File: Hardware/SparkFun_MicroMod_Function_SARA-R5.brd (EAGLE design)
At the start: 37.5 x 65 mm, 104 parts, among them IC2 SN74AVC4T774PW, J1 MICROMOD_FUNCTION_STANDARD, J2 U.FL, J5 U.FL, J9 NANO_SIM, Q2 310mA/60V/1.6Ω, Q3 310mA/60V/1.6Ω, Q5 310mA/60V/1.6Ω, Q6 310mA/60V/1.6Ω, U11 74HC1G04, U4 EEPROM, U6 LARA-R6001, U8 AP7361C-33FGE

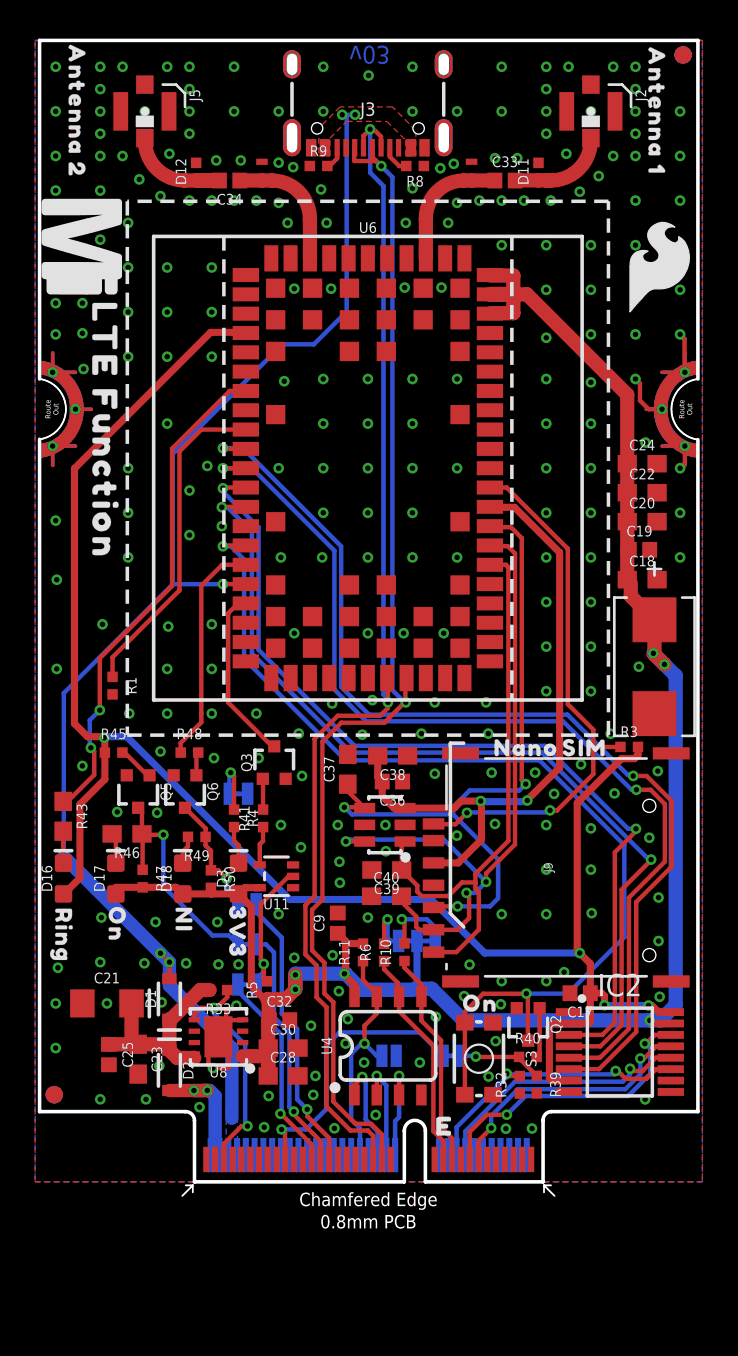
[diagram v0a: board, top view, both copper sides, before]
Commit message: added GNSS antenna U.FL
-added GNSS antenna U.FL, with supporting circuitry and power control
-rotated module 90 degrees
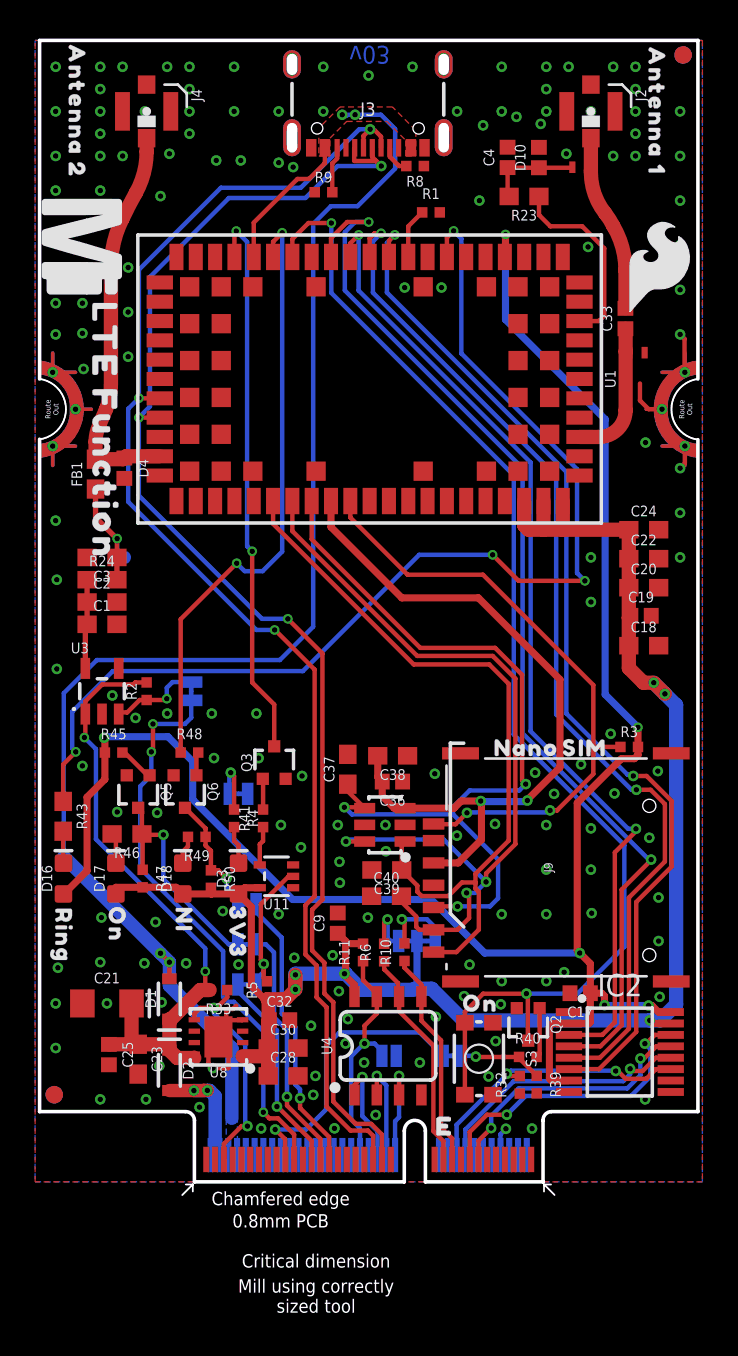
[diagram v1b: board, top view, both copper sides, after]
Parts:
- removed C16: T520D337M006ATE045, untitled:CAPMP7.6X4.3_3.1N_KEM
- removed C34: 33pF, New_Parts:0402
- removed D11, D12: PESD0402-0402T, SparkFun-DiscreteSemi:0402-TIGHT
- removed J5: U.FL, SparkFun-Connectors:U.FL
- removed U6: LARA-R6001, HPG_Solution:LARA-LGA
- added C1: 1.0uF, SparkFun-Capacitors:0603
- added C2: 0.1uF, SparkFun-Capacitors:0603
- added C3: 47pF, SparkFun-Capacitors:0603
- added C4: 27pF, New_Parts:0402
- added D10, D4: PESD0402, New_Parts:0402
- added FB1: 30Ω/1.8A, SparkFun-Coils:0603
- added J4: U.FL, SparkFun-Connectors:U.FL
- added JP4: JUMPER-SMT_2_NC_TRACE_SILK, SparkFun-Jumpers:SMT-JUMPER_2_NC_TRACE_SILK
- added R2: 100k, SparkFun-Resistors:0402-TIGHT
- added R23: 10k, SparkFun-Resistors:0603
- added R24: 10, SparkFun-Resistors:0603
- added TP22: TEST-POINT3, SparkFun-Connectors:PAD.03X.03
- added U1: SARA-R510M8S, SparkFun-RF:SARA-LGA
- added U3: 3.3V, SparkFun-IC-Power:SOT23-5
- JP3: value JUMPER-SMT_2_NO_SILK -> (none)
- L2: value DNP -> 68nH
- R46: device SparkFun-Resistors:0603 -> SparkFun-Resistors:0603@1
- moved R1 32.5 mm to (22.5, 55.2), turned to 0 degrees
- moved L2 18.1 mm to (31.0, 57.8), turned to 0 degrees
- moved L1 14.1 mm to (34.3, 47.2), turned to 0 degrees
- moved C33 10.4 mm to (33.6, 49.2), turned to 90 degrees
- moved C22 3.76 mm to (34.7, 35.5)
- moved C18 3.76 mm to (34.7, 30.5)
- moved C19 3.76 mm to (34.5, 32.2)
- moved C20 3.76 mm to (34.7, 33.8)
- moved C24 3.76 mm to (34.7, 37.1)
- moved R9 1.52 mm to (16.4, 56.4)
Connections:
- removed net LTE_ANT2: C34.1, L2.P$1, U6.62
- removed net N$10: C21.+, C23.1, C25.1, D1.C, D2.C, R33.2, U8.8
- removed net N$15: C33.2, D11.1, J2.FEED
- new net ANT_REG_EN: JP4.1, R2.1, U3.3
- new net GNSS_ANT: D4.1, FB1.2, J4.FEED, U1.31
- new net N$11: C33.2, J2.FEED, L2.P$2
- new net N$18: C4.1, D10.1, L2.P$1, R23.2
- new net N$24: C1.1, C2.1, R24.1, U3.5
- new net N$25: C3.1, FB1.1, R24.2, TP22.P$1
- new net SARA_ANT_DET: R23.1, U1.62
- new net VIN: C21.+, C23.1, C25.1, D1.C, D2.C, R2.2, R33.2, U3.1, U8.8
- net 3.3V: now also U1.51, U1.52, U1.53; no longer C16.1, U6.51, U6.52, U6.53
- net GND: now also C1.2, C2.2, C3.2, C4.2, D10.2, D4.2, J1.2, J1.8, J4.1, J4.2, U1.1, U1.14, U1.20, U1.21, U1.22, U1.3, U1.30, U1.32, U1.43, U1.5, U1.50, U1.54, U1.55, U1.57, U1.58, U1.59, U1.60, U1.61, U1.63, U1.64, U1.65, U1.66, U1.67, U1.68, U1.69, U1.70, U1.71, U1.72, U1.73, U1.74, U1.75, U1.76, U1.77, U1.78, U1.79, U1.80, U1.81, U1.82, U1.83, U1.84, U1.85, U1.86, U1.87, U1.88, U1.89, U1.90, U1.91, U1.92, U1.93, U1.94, U1.95, U1.96, U3.2; no longer C16.2, D11.2, D12.2, J5.1, J5.2, L2.P$2, U6.1, U6.14, U6.20, U6.21, U6.22, U6.3, U6.30, U6.32, U6.43, U6.5, U6.50, U6.54, U6.55, U6.57, U6.58, U6.60, U6.61, U6.63, U6.64, U6.65, U6.66, U6.67, U6.68, U6.69, U6.70, U6.71, U6.72, U6.73, U6.74, U6.75, U6.76, U6.77, U6.78, U6.79, U6.80, U6.81, U6.82, U6.83, U6.84, U6.85, U6.86, U6.87, U6.88, U6.89, U6.90, U6.91, U6.92, U6.93, U6.94, U6.95, U6.96
- net LTE_18_!RESET!: now also U1.18; no longer U6.18
- net LTE_18_CTS: now also U1.11; no longer U6.11
- net LTE_18_DTR: now also U1.9; no longer U6.9
- net LTE_18_NI: now also U1.16; no longer U6.16
- net LTE_18_PWR_ON: now also U1.15; no longer U6.15
- net LTE_18_RI: now also U1.7; no longer U6.7
- net LTE_18_RTS: now also U1.10; no longer U6.10
- net LTE_18_RXO: now also U1.13; no longer U6.13
- net LTE_18_TXI: now also U1.12; no longer U6.12
- net LTE_ANT: now also U1.56; no longer U6.56
- net N$4: now also J1.55, JP4.2; no longer C34.2, D12.1, J5.FEED
- net SIM_CLK: now also U1.38; no longer U6.38
- net SIM_DET: now also U1.42; no longer U6.42
- net SIM_IO: now also U1.39; no longer U6.39
- net SIM_RST: now also U1.40; no longer U6.40
- net USB_N: now also U1.28; no longer U6.28
- net USB_P: now also U1.29; no longer U6.29
- net VCCIO: now also U1.4; no longer U6.4
- net VSIM: now also U1.41; no longer U6.41
- net V_USB: now also U1.17; no longer U6.17
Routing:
- net VIN: track 0.00 -> 36.0 mm, vias 0 -> 2
- net LTE_18_RI: track 28.6 -> 63.7 mm, vias 2 -> 4
- net N$4: track 6.65 -> 32.5 mm, vias 0 -> 3
- net GNSS_ANT: track 0.00 -> 22.5 mm
- net LTE_18_NI: track 13.0 -> 35.1 mm, vias 0 -> 2
- net LTE_18_!RESET!: track 9.97 -> 31.8 mm, vias 0 -> 2
- net LTE_18_DTR: track 18.7 -> 2.87 mm
- net 3.3V: track 113.7 -> 99.4 mm
- net V_USB: track 75.6 -> 88.7 mm, vias 5 -> 4
- net N$10: track 12.6 -> 0.00 mm
- net LTE_18_PWR_ON: track 58.1 -> 69.8 mm
- net SARA_ANT_DET: track 0.00 -> 10.9 mm
- net SIM_CLK: track 32.8 -> 43.5 mm
- net USB_P: track 68.1 -> 78.8 mm, vias 2 -> 3
- net N$11: track 0.00 -> 10.5 mm
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
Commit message: Silk adjustments
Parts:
- removed U$19: (no value), output:ANTENNA_21212
- removed U$2: (no value), output:ANTENNA_121213
- added U$11: (no value), output:LTE_#_GNSS0
- added U$13: (no value), output:FUNCTION0
- added U$15: (no value), output:U#BLOX_SARA#R510M8S0
- added U$16: (no value), output:LTE0
- R46: device SparkFun-Resistors:0603@1 -> SparkFun-Resistors:0603
- U$17: device output:LTE_FUNCTION0 -> output:GNSS0
- moved U$12 21.6 mm to (10.0, 32.9), turned to 0 degrees
- moved LOGO2 20.0 mm to (29.3, 33.0)
- moved U$17 18.2 mm to (2.54, 61.0), turned to 90 degrees
- moved U$80 0.31 mm to (1.43, 14.3), turned to 90 degrees
- moved U$31 0.22 mm to (4.48, 14.8), turned to 90 degrees
- moved U$29 0.14 mm to (8.42, 15.0), turned to 90 degrees
- moved U$57 0.07 mm to (11.6, 14.2), turned to 90 degrees
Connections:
- net N$25: now also TP22.1; no longer TP22.P$1
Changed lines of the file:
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@@
 <setting verticaltext="up"/>
 </settings>
-<grid distance="0.05" unitdist="inch" unit="inch" style="lines" multiple="1" display="yes" altdistance="0.0001" altunitdist="inch" altunit="inch"/>
+<grid distance="0.05" unitdist="inch" unit="inch" style="lines" multiple="1" display="yes" altdistance="0.005" altunitdist="inch" altunit="inch"/>
 <layers>
 <layer number="1" name="Top" color="4" fill="1" visible="yes" active="yes"/>
@@
 <layer number="98" name="Guide" color="6" fill="1" visible="no" active="no"/>
 <layer number="99" name="SpiceOrder" color="7" fill="1" visible="no" active="no"/>
-<layer number="100" name="Muster" color="7" fill="1" visible="no" active="yes"/>
+<layer number="100" name="Muster" color="7" fill="1" visible="yes" active="yes"/>
 <layer number="101" name="Patch_Top" color="12" fill="4" visible="no" active="no"/>
 <layer number="102" name="Vscore" color="7" fill="1" visible="no" active="no"/>
@@
 <attribute name="VALUE" x="5.234" y="17.272" size="0.6096" layer="27" font="vector" ratio="20" rot="R90" align="top-center"/>
 </element>
-<element name="R46" library="SparkFun-Resistors" package="0603@1" value="100" x="5.234" y="19.812" smashed="yes" rot="R180">
+<element name="R46" library="SparkFun-Resistors" package="0603" value="100" x="5.234" y="19.812" smashed="yes" rot="R180">
 <attribute name="NAME" x="5.234" y="19.05" size="0.6096" layer="25" font="vector" ratio="20" rot="R180" align="bottom-center"/>
 <attribute name="PROD_ID" value="RES-07863" x="119.534" y="181.102" size="1.778" layer="27" font="vector" ratio="15" rot="R180" display="off"/>
@@
 <attribute name="VALUE" x="12.219" y="17.272" size="0.6096" layer="27" font="vector" ratio="20" rot="R90" align="top-center"/>
 </element>
-<element name="U$29" library="HPG_Solution" package="NI0" value="" x="8.4725" y="14.9225" smashed="yes" rot="R270"/>
-<element name="U$31" library="HPG_Solution" package="ON0" value="" x="4.6625" y="14.6685" smashed="yes" rot="R270"/>
-<element name="U$57" library="HPG_Solution" package="3V34" value="" x="11.5205" y="14.224" smashed="yes" rot="R270"/>
-<element name="U$80" library="output" package="RING0" value="" x="1.6145" y="14.0335" smashed="yes" rot="R270"/>
+<element name="U$29" library="HPG_Solution" package="NI0" value="" x="8.4185" y="15.0495" smashed="yes" rot="R90"/>
+<element name="U$31" library="HPG_Solution" package="ON0" value="" x="4.4815" y="14.7955" smashed="yes" rot="R90"/>
+<element name="U$57" library="HPG_Solution" package="3V34" value="" x="11.5935" y="14.224" smashed="yes" rot="R90"/>
+<element name="U$80" library="output" package="RING0" value="" x="1.4335" y="14.2875" smashed="yes" rot="R90"/>
 <element name="U$14" library="output" package="DESIGNED_BY_#MAZGCH_IN_SWITZERLAND3" value="" x="18.71311875" y="33.72611875" smashed="yes" rot="MR0"/>
 <element name="U$18" library="output" package="NANO0" value="" x="27.983184375" y="24.718340625" smashed="yes"/>
 <element name="U$126" library="output" package="SIM0" value="" x="31.295340625" y="24.708175" smashed="yes"/>
 <element name="U$5" library="HPG_Solution" package="ON0" value="" x="25.3492" y="10.1616" smashed="yes"/>
-<element name="U$12" library="SparkFun-MicroMod" package="MICROMOD_MI_LOGO_1" value="" x="2.694" y="53.213" smashed="yes" rot="R270"/>
-<element name="U$17" library="output" package="LTE_FUNCTION0" value="" x="3.964" y="42.799" smashed="yes" rot="R270"/>
-<element name="U$19" library="output" package="ANTENNA_21212" value="" x="2.3765" y="60.96" smashed="yes" rot="R270"/>
-<element name="U$2" library="output" package="ANTENNA_121213" value="" x="35.3965" y="60.96" smashed="yes" rot="R270"/>
+<element name="U$12" library="SparkFun-MicroMod" package="MICROMOD_MI_LOGO_1" value="" x="10.033" y="32.92" smashed="yes"/>
 <element name="J2" library="SparkFun-Connectors" package="U.FL" value="U.FL" x="31.65" y="60.96" smashed="yes" rot="R270">
 <attribute name="NAME" x="34.19" y="62.23" size="0.6096" layer="25" font="vector" ratio="20" rot="R270"/>
@@
 <element name="U$3" library="SparkFun-MicroMod" package="MICROMOD_MI_LOGO_1" value="" x="18.026378125" y="41.7465" smashed="yes" rot="MR0"/>
 <element name="U$4" library="output" package="LTE_FUNCTION0" value="" x="17.848584375" y="37.321821875" smashed="yes" rot="MR0"/>
-<element name="LOGO2" library="SparkFun-Aesthetics" package="SFE_LOGO_FLAME_.2" value="SFE_LOGO_FLAME.2_INCH" x="35.56" y="52.07" smashed="yes"/>
+<element name="LOGO2" library="SparkFun-Aesthetics" package="SFE_LOGO_FLAME_.2" value="SFE_LOGO_FLAME.2_INCH" x="29.337" y="33.02" smashed="yes"/>
 <element name="R5" library="SparkFun-Resistors" package="0402-TIGHT" value="100k" x="13.208" y="10.922" smashed="yes" rot="R90">
 <attribute name="NAME" x="12.646" y="10.922" size="0.6096" layer="25" font="vector" ratio="20" rot="R90" align="bottom-center"/>
@@
 <attribute name="VALUE" x="29.4513" y="58.331096875" size="0.6096" layer="27" font="vector" ratio="20" rot="R90" align="top-center"/>
 </element>
+<element name="U$11" library="output" package="LTE_#_GNSS0" value="" x="20.32" y="34.036" smashed="yes"/>
+<element name="U$13" library="output" package="FUNCTION0" value="" x="20.193" y="31.75" smashed="yes"/>
+<element name="U$15" library="output" package="U#BLOX_SARA#R510M8S0" value="" x="19.685" y="29.21" smashed="yes"/>
+<element name="U$16" library="output" package="LTE0" value="" x="35.56" y="60.96" smashed="yes" rot="R90"/>
+<element name="U$17" library="output" package="GNSS0" value="" x="2.54" y="60.96" smashed="yes" rot="R90"/>
 </elements>
 <signals>
@@
 <contactref element="FB1" pad="1"/>
 <contactref element="C3" pad="1"/>
-<contactref element="TP22" pad="P$1"/>
+<contactref element="TP22" pad="1"/>
 <wire x1="4.66" y1="34.29" x2="4.66" y2="35.56" width="0.3048" layer="1"/>
 <wire x1="3.4417" y1="37.839121875" x2="3.4417" y2="39.452178125" width="0.3048" layer="1"/>
@@
 </signals>
 <mfgpreviewcolors>
-<mfgpreviewcolor name="soldermaskcolor" color="0xC8008000"/>
-<mfgpreviewcolor name="silkscreencolor" color="0xFFFEFEFE"/>
+<mfgpreviewcolor name="soldermaskcolor" color="0xC8AA0000"/>
+<mfgpreviewcolor name="silkscreencolor" color="0xFFFFFFFF"/>
 <mfgpreviewcolor name="backgroundcolor" color="0xFF282828"/>
 <mfgpreviewcolor name="coppercolor" color="0xFFFFBF00"/>

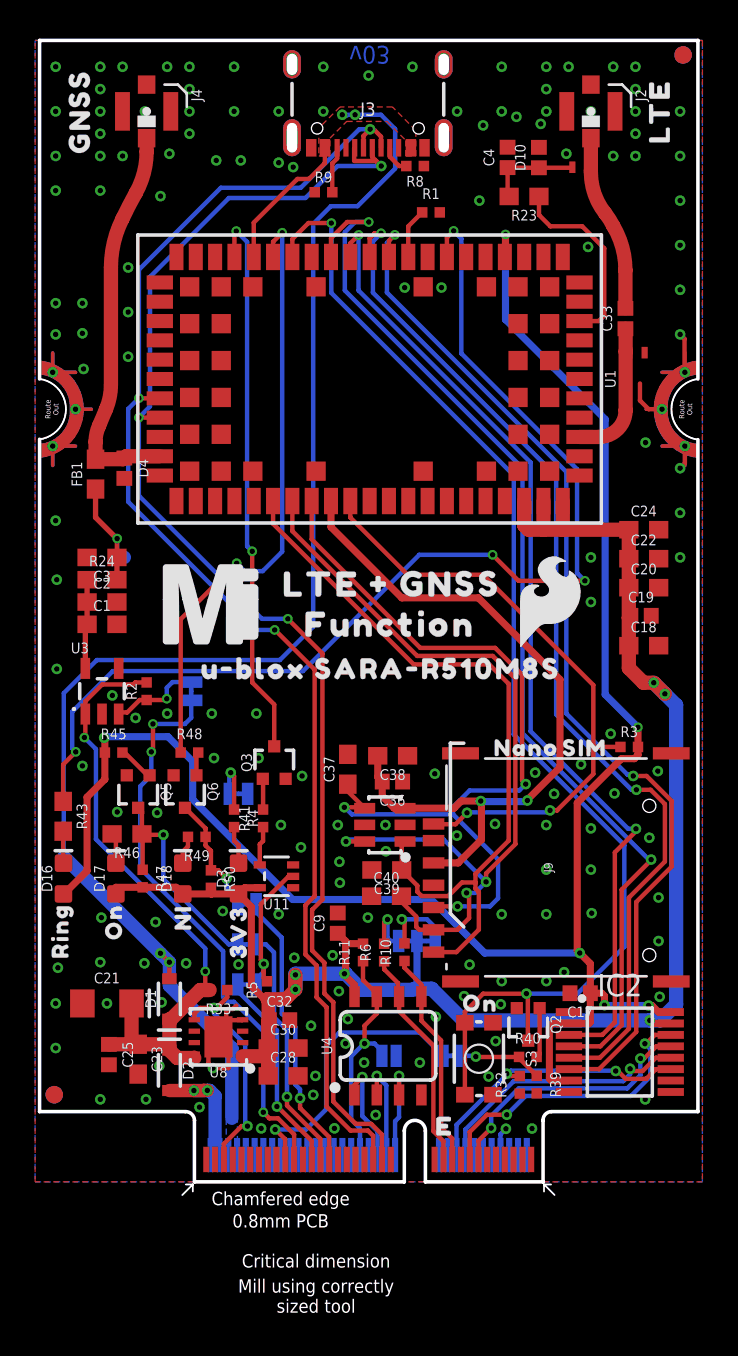
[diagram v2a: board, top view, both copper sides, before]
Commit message: Increase VUSB trace to 30mil
-u.fl FP library update - adds restrict underneath
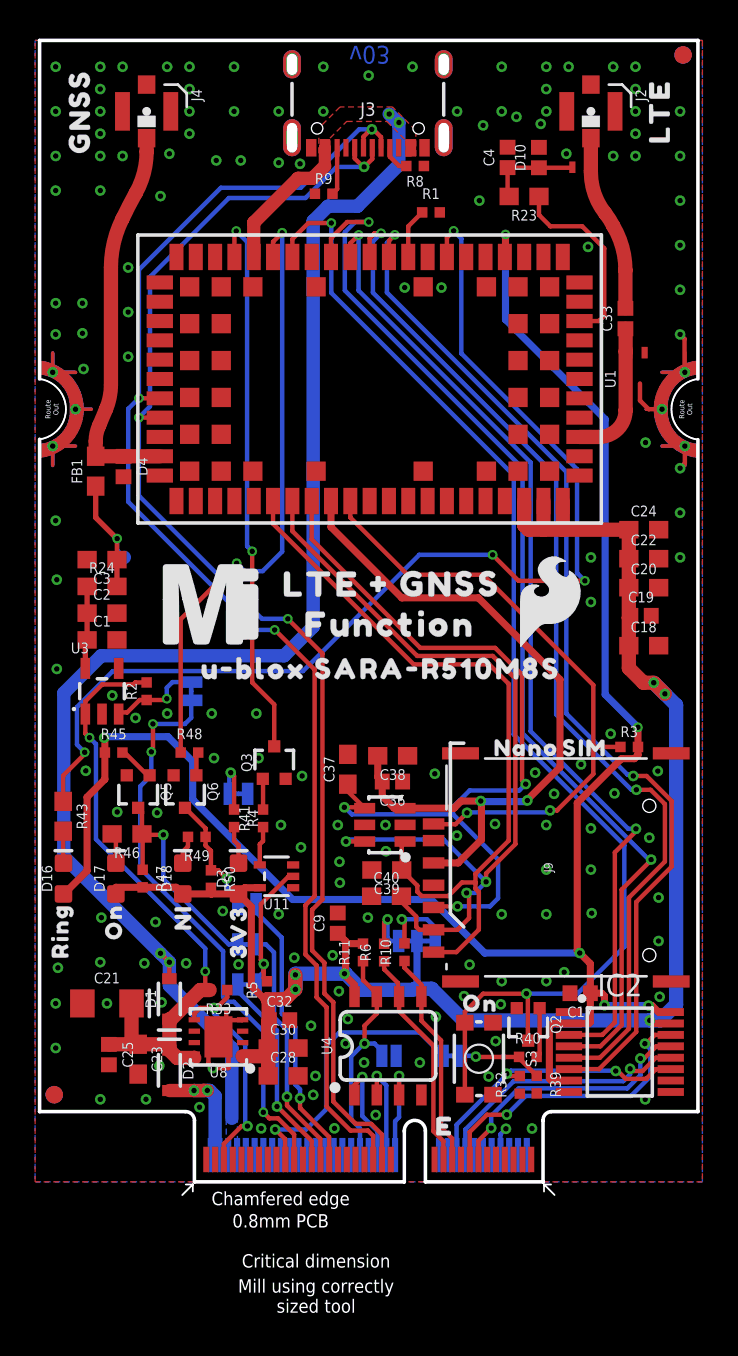
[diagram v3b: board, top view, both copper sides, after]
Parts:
- C20: device SparkFun-Capacitors:0603@1 -> SparkFun-Capacitors:0603
- moved C1 0.89 mm to (3.81, 30.9)
- moved C2 0.64 mm to (3.81, 32.4)
- moved R24 0.38 mm to (3.81, 33.9)
- moved FB1 0.17 mm to (3.45, 40.5)
- moved C3 0.13 mm to (3.81, 35.4)
- moved D4 0.11 mm to (5.03, 40.7)
- moved R9 0.08 mm to (16.4, 56.3)
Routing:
- net V_USB: track 88.7 -> 86.5 mm
- net USB_P: track 78.8 -> 76.7 mm
- net GND: track 19.7 -> 19.0 mm, vias 159 -> 157
- net N$25: track 6.92 -> 7.47 mm
